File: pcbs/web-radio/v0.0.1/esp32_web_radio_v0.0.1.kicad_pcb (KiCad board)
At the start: 4 copper layers, 52.5 x 42 mm, 62 parts, among them J2 Conn_01x05_Pin, J3 USB4085-GF-A_REVB, J4 Conn_01x02_Pin, SW1 BOOT, SW2 RESET, SW3 VOLUME_UP, SW7 VOLUME_DOWN, SW8 MUTE, U1 TLV320AIC3100, U2 ESP32-S3-WROOM-1, U3 AP2127K-1.8, U4 LD39200PUR

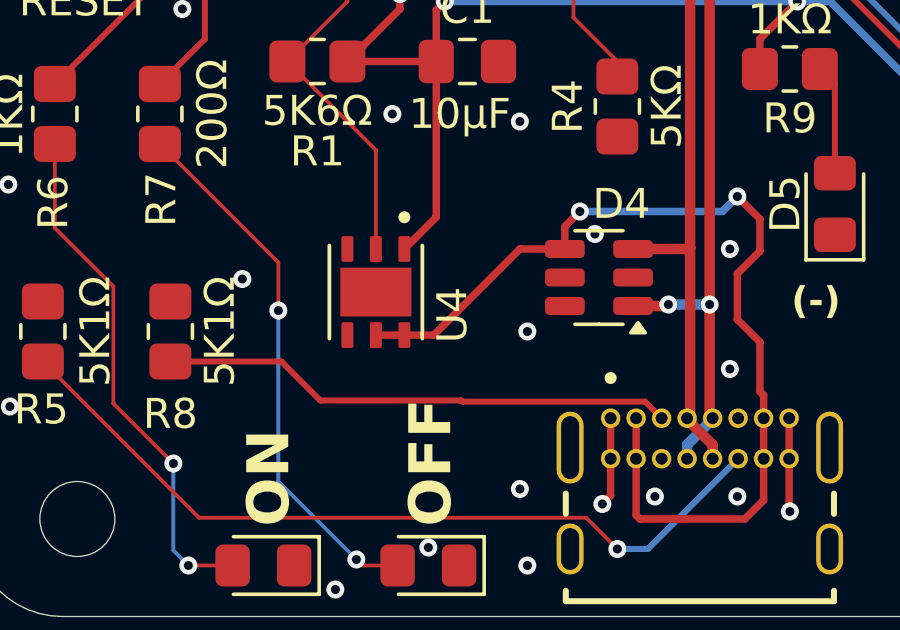
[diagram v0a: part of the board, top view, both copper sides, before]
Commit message: adding libraries
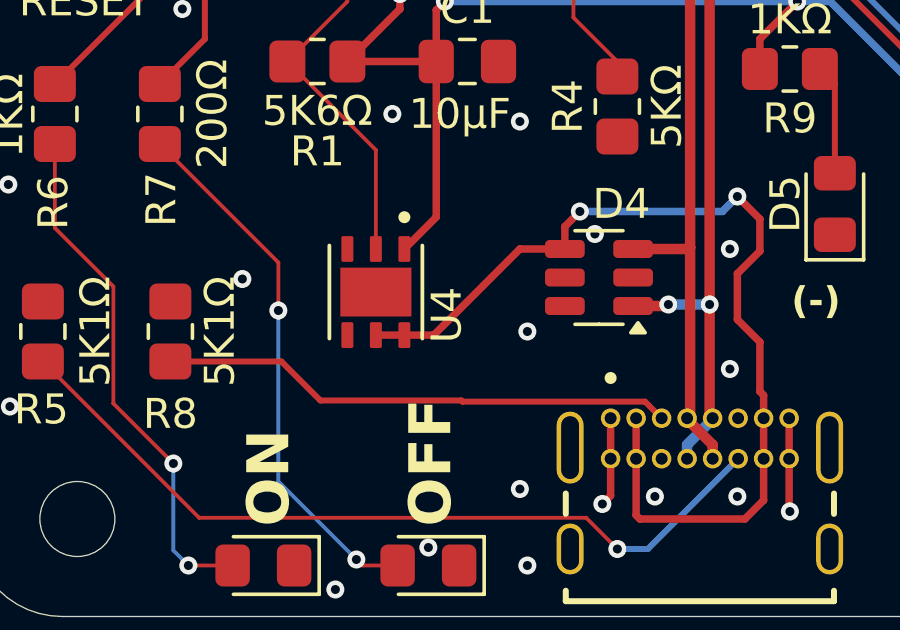
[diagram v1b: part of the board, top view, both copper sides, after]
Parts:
- J3: footprint USB4085-GF-A_REVB:GCT_USB4085-GF-A_REVB -> smallest-space-hardware/libs:GCT_USB4085-GF-A_REVB
- U4: footprint LD39200PUR:SON95P300X300X100-7N -> smallest-space-hardware/libs:SON95P300X300X100-7N

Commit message: fix libraries and update schematics
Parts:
- removed the C18 at (222.4, 137.0)
- removed the C20 at (222.4, 143.1)
- removed the C21 at (222.4, 146.1)
- removed the C22 at (222.4, 149.1)
- removed J4: Conn_01x02_Pin, Connector_JST:JST_PH_S2B-PH-SM4-TB_1x02-1MP_P2.00mm_Horizontal
- removed the R13 at (186.4, 128.4)
- removed the R14 at (186.4, 131.4)
- removed the R15 at (186.4, 134.3)
- removed R16, R17: 10KΩ, Resistor_SMD:R_0805_2012Metric_Pad1.20x1.40mm_HandSolder
- removed SW7: VOLUME_DOWN, Button_Switch_SMD:SW_SPST_PTS810
- removed SW8: MUTE, Button_Switch_SMD:SW_SPST_PTS810
- added C1: 100µF, Capacitor_SMD:C_1206_3216Metric_Pad1.33x1.80mm_HandSolder, F.Cu at (191.5, 139.5)
- added C10: 22µF, Capacitor_SMD:C_0805_2012Metric_Pad1.18x1.45mm_HandSolder, F.Cu at (195.7, 117.0)
- added C2: 100µF, Capacitor_SMD:C_0805_2012Metric_Pad1.18x1.45mm_HandSolder, F.Cu at (190.9, 114.0)
- added C4: 22µF, Capacitor_SMD:C_0805_2012Metric_Pad1.18x1.45mm_HandSolder, F.Cu at (190.9, 117.0)
- added C5: 10µF, Capacitor_SMD:C_0805_2012Metric_Pad1.18x1.45mm_HandSolder, F.Cu at (190.9, 120.0)
- added C9: 0.1µF, Capacitor_SMD:C_0805_2012Metric_Pad1.18x1.45mm_HandSolder, F.Cu at (195.7, 114.0)
- added J3: Conn_01x02_Pin, Connector_JST:JST_PH_S2B-PH-SM4-TB_1x02-1MP_P2.00mm_Horizontal, F.Cu at (208.1, 135.8)
- added R1: 4K7Ω, Resistor_SMD:R_0805_2012Metric_Pad1.20x1.40mm_HandSolder, F.Cu at (205.3, 114.0)
- added R11: 10KΩ, Resistor_SMD:R_0805_2012Metric_Pad1.20x1.40mm_HandSolder, F.Cu at (205.3, 125.8)
- added R12: 10KΩ, Resistor_SMD:R_0805_2012Metric_Pad1.20x1.40mm_HandSolder, F.Cu at (205.3, 128.7)
- added R8: 10KΩ, Resistor_SMD:R_0805_2012Metric_Pad1.20x1.40mm_HandSolder, F.Cu at (205.3, 119.9)
- added R9: 10KΩ, Resistor_SMD:R_0805_2012Metric_Pad1.20x1.40mm_HandSolder, F.Cu at (205.3, 122.8)
- added SW2: VOLUME_UP, Button_Switch_SMD:SW_SPST_PTS810, F.Cu at (211.1, 114.9)
- added SW4: MUTE, Button_Switch_SMD:SW_SPST_PTS810, F.Cu at (211.1, 124.4)
- C11, C14: value 22µF -> 0.1µF
- C19: value 10µF -> 0.1µF
- C8: value 0.1µF -> 10µF
- J1: renamed from J3; footprint smallest-space-hardware/libs:GCT_USB4085-GF-A_REVB -> smallest.space:GCT_USB4085-GF-A_REVB
- R7: value 4K7Ω -> 10KΩ
- SW3: value VOLUME_UP -> VOLUME_DOWN
- U1: value TLV320AIC3100 -> AP2127K-1.8; footprint Package_DFN_QFN:VQFN-32-1EP_5x5mm_P0.5mm_EP3.5x3.5mm -> Package_TO_SOT_SMD:SOT-23-5
- U2: renamed from U4; footprint smallest-space-hardware/libs:SON95P300X300X100-7N -> smallest.space:SON95P300X300X100-7N
- U3: value AP2127K-1.8 -> TLV320DAC3100; footprint Package_TO_SOT_SMD:SOT-23-5 -> Package_DFN_QFN:VQFN-32-1EP_5x5mm_P0.5mm_EP3.5x3.5mm
- moved C13 29.4 mm to (195.7, 126.0)
- moved C11 29.4 mm to (195.7, 120.0)
- moved C12 29.4 mm to (195.7, 123.0)
- moved C14 29.4 mm to (195.7, 129.1)
- moved C19 27.7 mm to (200.5, 123.0)
- moved C15 26.0 mm to (200.5, 114.0)
- moved C17 26.0 mm to (200.5, 120.0)
- moved C16 26.0 mm to (200.5, 117.0)
- moved R7 20.8 mm to (205.3, 116.9)
- moved SW3 20.1 mm to (211.1, 119.6)
- moved C6 15.4 mm to (190.9, 123.0)
- moved C8 15.4 mm to (190.9, 129.1)
- moved C7 15.4 mm to (190.9, 126.0)
- moved U1 8.16 mm to (198.7, 133.0)
- moved U3 6.57 mm to (192.5, 134.2)
- renumbered C4 to C18, C5 to C20, C2 to C21, C3 to C22, C1 to C3, D5 to D1, D4 to D2, D1 to D3, H3 to H2, H2 to H3, R6 to R10, R3 to R13, R12 to R14, R4 to R15, R8 to R2, R5 to R3, R9 to R4, R1 to R5, R2 to R6, SW2 to SW5, SW1 to SW6, U2 to U4
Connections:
- C11 pad 1: Net-(C11-Pad1) -> VOLUME_UP
- C11 pad 2: +5V -> GND
- C12 pad 1: Net-(C11-Pad1) -> VOLUME_DOWN
- C12 pad 2: +5V -> GND
- C13 pad 1: Net-(C13-Pad1) -> MUTE
- C13 pad 2: +5V -> GND
- C14 pad 1: Net-(C13-Pad1) -> IOVDD
- C14 pad 2: +5V -> +3.3V
- C15 pad 1: DVDD -> Net-(C15-Pad1)
- C15 pad 2: +1.8V -> +5V
- C16 pad 1: DVDD -> Net-(C15-Pad1)
- C16 pad 2: +1.8V -> +5V
- C17 pad 1: IOVDD -> Net-(C17-Pad1)
- C17 pad 2: +3.3V -> +5V
- C19 pad 1: HPVDD -> Net-(C17-Pad1)
- C19 pad 2: +3.3V -> +5V
- C6 pad 1: VOLUME_UP -> DVDD
- C6 pad 2: GND -> +1.8V
- C7 pad 1: VOLUME_DOWN -> HPVDD
- C7 pad 2: GND -> +3.3V
- C8 pad 1: MUTE -> AVDD
- C8 pad 2: GND -> +3.3V
- D3 pad 2: Net-(D1-A) (its old number) -> Net-(D3-A)
- R10 pad 1: Net-(D1-A) (its old number) -> Net-(D3-A)
- R7 pad 1: Net-(R7-Pad1) -> +3.3V
- R7 pad 2: +5V -> SDA
- SW3 pad 2: VOLUME_UP -> VOLUME_DOWN
- U1 pad 1: GND -> +5V
- U1 pad 2: IOVDD -> GND
- U1 pad 3: DVDD -> ENABLED_SWITCH
- U1 pad 4: DOUT -> unconnected-(U1-NC-Pad4)
- U1 pad 5: DIN -> +1.8V
- U2 pad 5: /ENABLE_SWITCH -> ENABLED_SWITCH
- U3 pad 1: +5V -> GND
- U3 pad 2: GND -> IOVDD
- U3 pad 3: ENABLED_SWITCH -> DVDD
- U3 pad 5: +1.8V -> DIN
- U4 pad 12: DOUT -> unconnected-(U4-IO8-Pad12)
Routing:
- net Net-(D3-A): track 3.43 -> 20.8 mm, vias 1 -> 3
- net Net-(D1-A) (its old number): track 17.4 -> 0.00 mm, vias 2 -> 0

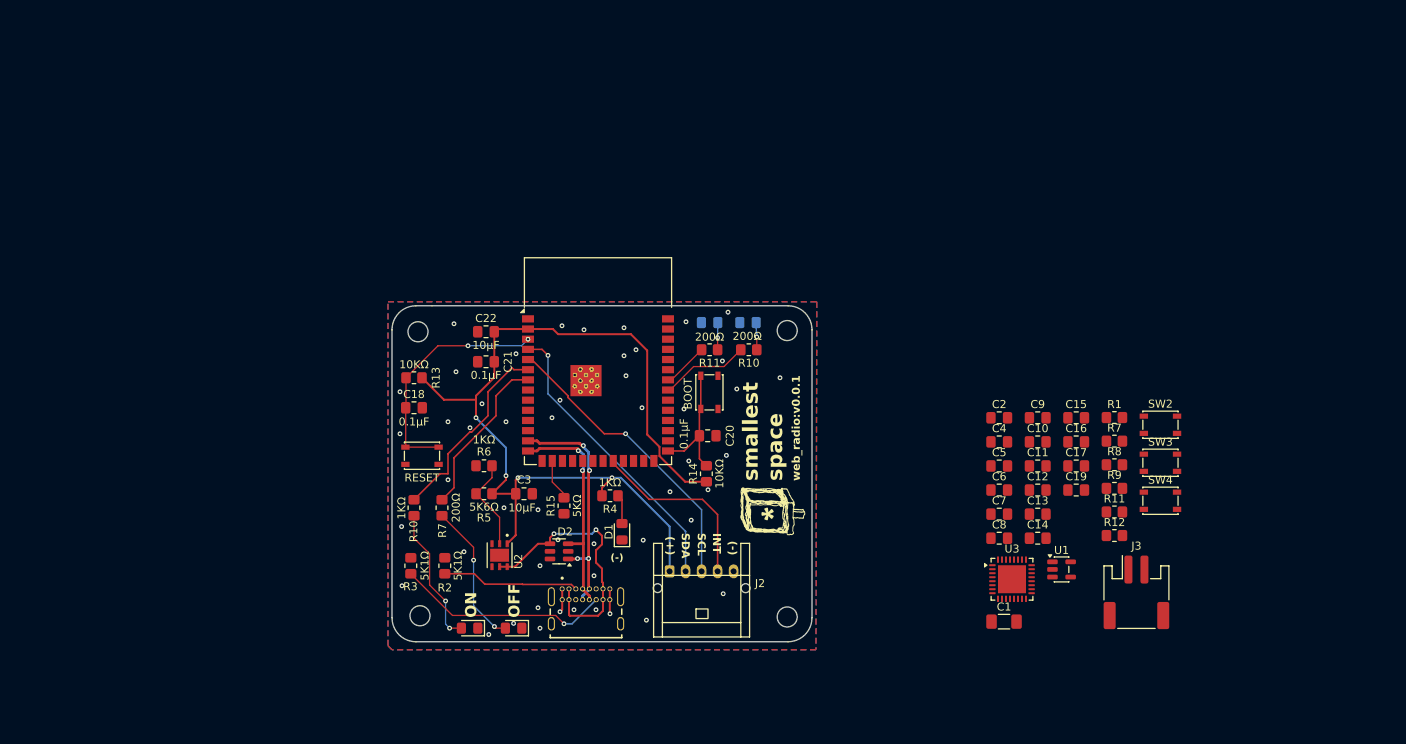
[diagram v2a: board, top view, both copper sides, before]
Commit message: switching to some 0603 passives
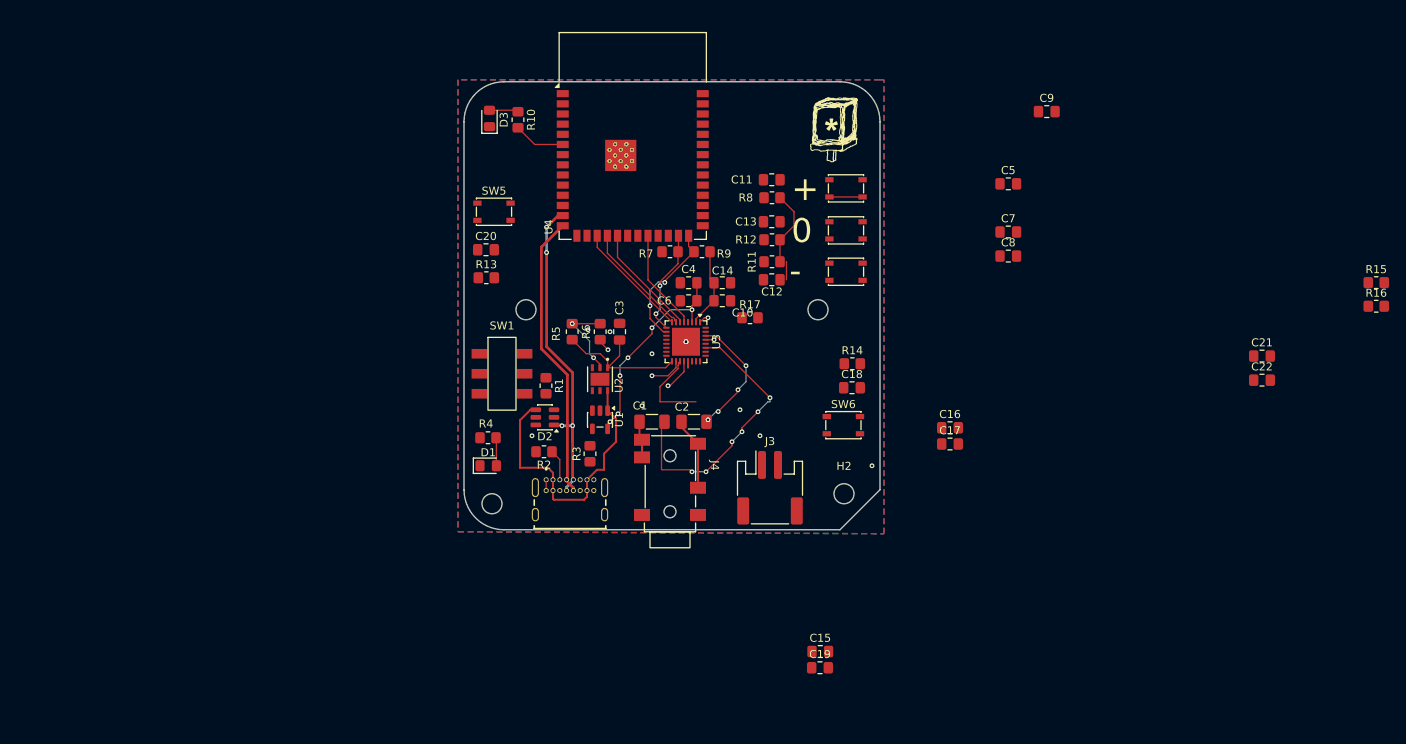
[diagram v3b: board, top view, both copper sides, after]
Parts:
- removed the D2 at (130.2, 140.3)
- removed the D2 at (135.9, 130.7)
- removed the D3 at (124.7, 140.3)
- removed the D3 at (159.5, 102.1)
- removed D6: DISABLED, LED_SMD:LED_0805_2012Metric_Pad1.15x1.40mm_HandSolder
- removed the G*** at (162.6, 125.7)
- removed the G*** at (146.8, 127.5)
- removed J2: Conn_01x05_Pin, smallest-space-footprints:JST_S05B-PASK-2_1x05_P2.00mm_Side_entry
- removed the R10 at (117.8, 125.2)
- removed the R10 at (159.6, 105.5)
- removed the R11 at (205.3, 125.8)
- removed the R11 at (154.7, 105.5)
- removed the R7 at (121.2, 125.2)
- removed the R7 at (205.3, 116.9)
- added D2: ESDA6V1BC6, Package_TO_SOT_SMD:SOT-23-6, F.Cu at (134.1, 114.0)
- added D3: STATUS, LED_SMD:LED_0805_2012Metric_Pad1.15x1.40mm_HandSolder, F.Cu at (127.2, 76.6)
- added G***: LOGO, smallest.space:smallest_space_1, F.Cu at (170.2, 78.0)
- added J4: AudioJack4_4C_54-00177, smallest.space:54-00177-headphone-3.5mm-jack, F.Cu at (149.8, 121.8)
- added R10: 1KΩ, Resistor_SMD:R_0805_2012Metric_Pad1.20x1.40mm_HandSolder, F.Cu at (130.8, 76.8)
- added R11: 10KΩ, Resistor_SMD:R_0805_2012Metric_Pad1.20x1.40mm_HandSolder, F.Cu at (162.5, 94.5)
- added R16: 10KΩ, Resistor_SMD:R_0805_2012Metric_Pad1.20x1.40mm_HandSolder, F.Cu at (238.0, 100.1)
- added R17: 10KΩ, Resistor_SMD:R_0805_2012Metric_Pad1.20x1.40mm_HandSolder, F.Cu at (159.8, 101.5)
- added R7: 10KΩ, Resistor_SMD:R_0805_2012Metric_Pad1.20x1.40mm_HandSolder, F.Cu at (149.8, 93.2)
- added SW1: SW_Slide_DPDT, smallest.space:SLW-913535-2A-SMT, F.Cu at (128.8, 108.5)
- C2: footprint Capacitor_SMD:C_0805_2012Metric_Pad1.18x1.45mm_HandSolder -> Capacitor_SMD:C_1206_3216Metric_Pad1.33x1.80mm_HandSolder
- moved R15 105.3 mm to (238.0, 97.1), turned to 0 degrees
- moved C22 97.2 mm to (223.8, 109.3)
- moved C21 97.0 mm to (223.8, 106.3)
- moved R1 71.2 mm to (134.2, 110.0), turned to -90 degrees
- moved H4 62.8 mm to (168.2, 100.5)
- moved U1 60.7 mm to (141.0, 114.2), turned to -90 degrees
- moved R9 59.4 mm to (153.8, 93.2), turned to 180 degrees
- moved R12 56.6 mm to (162.5, 91.8), turned to 180 degrees
- moved C18 54.8 mm to (172.5, 110.2)
- moved R8 54.3 mm to (162.5, 86.5), turned to 180 degrees
- moved SW4 51.8 mm to (171.8, 90.6)
- moved C14 50.7 mm to (156.3, 97.1), turned to 180 degrees
- moved C1 50.6 mm to (147.5, 114.5)
- moved U3 50.4 mm to (151.8, 104.5), turned to -90 degrees
- moved H3 50.4 mm to (131.8, 100.5)
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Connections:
- C10 pad 1: IOVDD -> GND
- C14 pad 1: IOVDD -> GND
- C15 pad 1: Net-(C15-Pad1) -> GND
- C16 pad 1: Net-(C15-Pad1) -> GND
- C17 pad 1: Net-(C17-Pad1) -> GND
- C19 pad 1: Net-(C17-Pad1) -> GND
- C4 pad 1: DVDD -> GND
- C5 pad 1: HPVDD -> GND
- C6 pad 1: DVDD -> GND
- C7 pad 1: HPVDD -> GND
- C8 pad 1: AVDD -> GND
- C9 pad 1: AVDD -> GND
- U3 pad 17: AVDD -> +3.3V
- U3 pad 2: IOVDD -> +3.3V
- U3 pad 21: Net-(C15-Pad1) -> +5V
- U3 pad 24: Net-(C17-Pad1) -> +5V
- U3 pad 28: HPVDD -> +3.3V
- U3 pad 3: DVDD -> +1.8V
- U3 pad 32: GPIO1 -> Net-(U3-GPIO1)
- U4 pad 17: BCLK -> MCLK
- U4 pad 18: WCLK -> BCLK
- U4 pad 19: MCLK -> WCLK
- U4 pad 20: GPIO1 -> unconnected-(U4-IO12-Pad20)
- U4 pad 22: unconnected-(U4-IO14-Pad22) -> DIN
- U4 pad 25: unconnected-(U4-IO48-Pad25) -> SDA
- U4 pad 26: unconnected-(U4-IO45-Pad26) -> SCL
- U4 pad 4: SDA -> unconnected-(U4-IO4-Pad4)
- U4 pad 5: SCL -> unconnected-(U4-IO5-Pad5)
- U4 pad 7: DIN -> unconnected-(U4-IO7-Pad7)
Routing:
- net +3.3V: track 114.4 -> 38.4 mm, vias 4 -> 0
- net /GPIO5: track 37.3 -> 0.00 mm, vias 1 -> 0
- net /GPIO4: track 36.9 -> 0.00 mm, vias 1 -> 0
- net HEADPHONE_LEFT: track 0.00 -> 35.1 mm, vias 0 -> 6
- net Net-(U4-EN): track 30.1 -> 0.00 mm, vias 2 -> 0
- net Net-(J1-CC2): track 27.0 -> 0.00 mm, vias 1 -> 0
- net +1.8V: track 0.00 -> 26.0 mm, vias 0 -> 6
- net /GPIO12: track 23.1 -> 0.00 mm
- net /LED_DISABLED: track 20.6 -> 0.00 mm
- net Net-(D2-A): track 18.0 -> 0.00 mm, vias 2 -> 0
- net STATUS: track 24.4 -> 6.46 mm
- net Net-(D3-A): track 20.8 -> 3.64 mm, vias 3 -> 0
- net Net-(U4-IO0): track 16.4 -> 0.00 mm
- net SCL: track 0.00 -> 16.2 mm, vias 0 -> 2
- net HEADPHONE_RIGHT: track 0.00 -> 15.8 mm, vias 0 -> 4
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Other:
- board size 52.5 x 42 mm -> 52 x 56 mm
- board text added: "+"
- board text added: "-"
- board text added: "0"
- board text removed: "(+)"
- board text removed: "(-)"
- board text removed: "DISABLED"
- board text removed: "ENABLED"
- board text removed: "INT"
- board text removed: "OFF"
- board text removed: "ON"
- board text removed: "SCL"
- board text removed: "SDA"
- board text removed: "github.com/kevin-mitchell/smallest-space-hardware /tree/main/pcbs/main/v0.3.1"
- board text removed: "main:v0.3.1"
- board text removed: "smallest space"
- board text removed: "web_radio:v0.0.1"

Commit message: add version 1
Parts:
- added G***: LOGO, smallest.space:smallest_space_1, B.Cu at (123.5, 78.8)
- added J2: Conn_01x01_Pin, TestPoint:TestPoint_Pad_1.0x1.0mm, F.Cu at (89.5, 105.2)
- added J5: Conn_01x01_Pin, TestPoint:TestPoint_Pad_1.0x1.0mm, F.Cu at (95.0, 119.5)
- added J6: Conn_01x01_Pin, TestPoint:TestPoint_Pad_1.0x1.0mm, F.Cu at (121.2, 99.8)
- C10, C14, C15, C16, C17, C19, C4, C5, C6, C7, C8, C9: footprint Capacitor_SMD:C_0805_2012Metric_Pad1.18x1.45mm_HandSolder -> Capacitor_SMD:C_0603_1608Metric_Pad1.08x0.95mm_HandSolder
- H1, H2, H3, H4: footprint MountingHole:MountingHole_2.5mm -> MountingHole:MountingHole_2.7mm
- moved R15 156.4 mm to (81.8, 91.8)
- moved C22 150.9 mm to (77.0, 74.2)
- moved C21 150.8 mm to (77.0, 71.8)
- moved R16 129.7 mm to (108.5, 93.5), turned to 180 degrees
- moved C9 102.7 mm to (99.6, 109.0)
- moved C18 99.9 mm to (74.8, 89.5)
- moved C8 93.8 mm to (99.2, 107.5)
- moved G*** 90.7 mm to (82.2, 100.0)
- moved C5 84.7 mm to (109.8, 104.8), turned to 180 degrees
- moved C7 83.5 mm to (110.0, 106.2), turned to 180 degrees
- moved C16 82.3 mm to (102.5, 111.8), turned to 90 degrees
- moved R9 80.1 mm to (75.0, 78.8), turned to 0 degrees
- moved C17 77.6 mm to (107.5, 109.5), turned to 180 degrees
- moved R7 74.7 mm to (77.0, 76.5)
- moved C15 72.4 mm to (104.0, 110.5), turned to 90 degrees
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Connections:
- U4 pad 17: MCLK -> unconnected-(U4-IO9-Pad17)
- U4 pad 18: BCLK -> unconnected-(U4-IO10-Pad18)
- U4 pad 19: WCLK -> SCL
- U4 pad 20: unconnected-(U4-IO12-Pad20) -> SDA
- U4 pad 21: AUDIO_RESET -> unconnected-(U4-IO13-Pad21)
- U4 pad 22: DIN -> MCLK
- U4 pad 23: unconnected-(U4-IO21-Pad23) -> BCLK
- U4 pad 24: unconnected-(U4-IO47-Pad24) -> WCLK
- U4 pad 25: SDA -> DIN
- U4 pad 26: SCL -> AUDIO_RESET
- U4 pad 31: unconnected-(U4-IO38-Pad31) -> VOLUME_DOWN
- U4 pad 34: VOLUME_DOWN -> unconnected-(U4-IO41-Pad34)
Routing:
- net +3.3V: track 38.4 -> 233.3 mm, vias 0 -> 9
- net ENABLED_SWITCH: track 0.00 -> 83.1 mm, vias 0 -> 2
- net +5V: track 37.1 -> 109.8 mm, vias 0 -> 10
- net Net-(U4-IO0): track 0.00 -> 56.2 mm
- net AUDIO_RESET: track 0.00 -> 45.8 mm, vias 0 -> 4
- net MUTE: track 0.00 -> 42.8 mm, vias 0 -> 2
- net VOLUME_UP: track 4.15 -> 40.8 mm
- net VOLUME_DOWN: track 2.27 -> 37.7 mm, vias 0 -> 2
- net Net-(J3-Pin_2): track 0.00 -> 33.4 mm, vias 0 -> 6
- net SDA: track 13.2 -> 41.6 mm
- net Net-(U4-EN): track 0.00 -> 26.2 mm
- net SCL: track 16.2 -> 41.3 mm
- net HEADPHONE_LEFT: track 35.1 -> 13.3 mm, vias 6 -> 2
- net Net-(J3-Pin_1): track 10.6 -> 27.7 mm
- net STATUS: track 6.46 -> 22.6 mm
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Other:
- board size 52 x 56 mm -> 60 x 60 mm
- rule pad_to_mask_clearance: 0 -> 0.05
- rule solder_mask_min_width: 0.12 -> 0.1
- board text added: "++"
- board text added: "--"
- board text added: "0/1"
- board text added: "1V8"
- board text added: "3V3"
- board text added: "5V"
- board text added: "5s ="
- board text added: "off"
- board text added: "on"
- board text added: "power"
- board text added: "reset"
- board text added: "restart"
- board text added: "smallest space"
- board text added: "status"
- board text added: "web radio v0.0.1"
- board text removed: "+"
- board text removed: "-"
- board text removed: "0"
